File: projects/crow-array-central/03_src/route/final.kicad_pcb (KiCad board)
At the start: 6 copper layers, 176 x 122 mm, 238 parts, among them J1 RJHSE-5384, J10 INJ IN, J11 5V TERM DNP, J12 USB4105-GF-A, J13 xSYS DBG TDI/TDO, J14 xSYS DBG TMS/TCK, J2 RJHSE-5384, J3 RJHSE-5384, J4 RJHSE-5384, J5 RJHSE-5384, J6 RJHSE-5384, J7 RJHSE-5384 DNP, J8 RJHSE-5384 DNP, J9 DC-005 5V IN, Q1 AO3400A beep 1, Q2 AO3400A beep 2, Q3 AO3400A beep 3, Q4 AO3400A beep 4, Q5 AO3400A beep 5, Q6 AO3400A beep 6, Q7 AO3400A beep 7, Q8 AO3400A beep 8, Q9 AO3401A revFET, U1 XU316-1024-TQ128-I24, U10 AP61102 3V3, U11 AP61102 0V9, U12 TCR2LF18 1V8, U13 XC6227 3V3A, U2 PCM1865DBTR, U3 PCM1865DBTR, U4 W25Q16JVSSIQ, U5 NC7NZ34 MCLK buf, U6 SHT40-AD1B (0x44), Y1 FA-238 24MHz

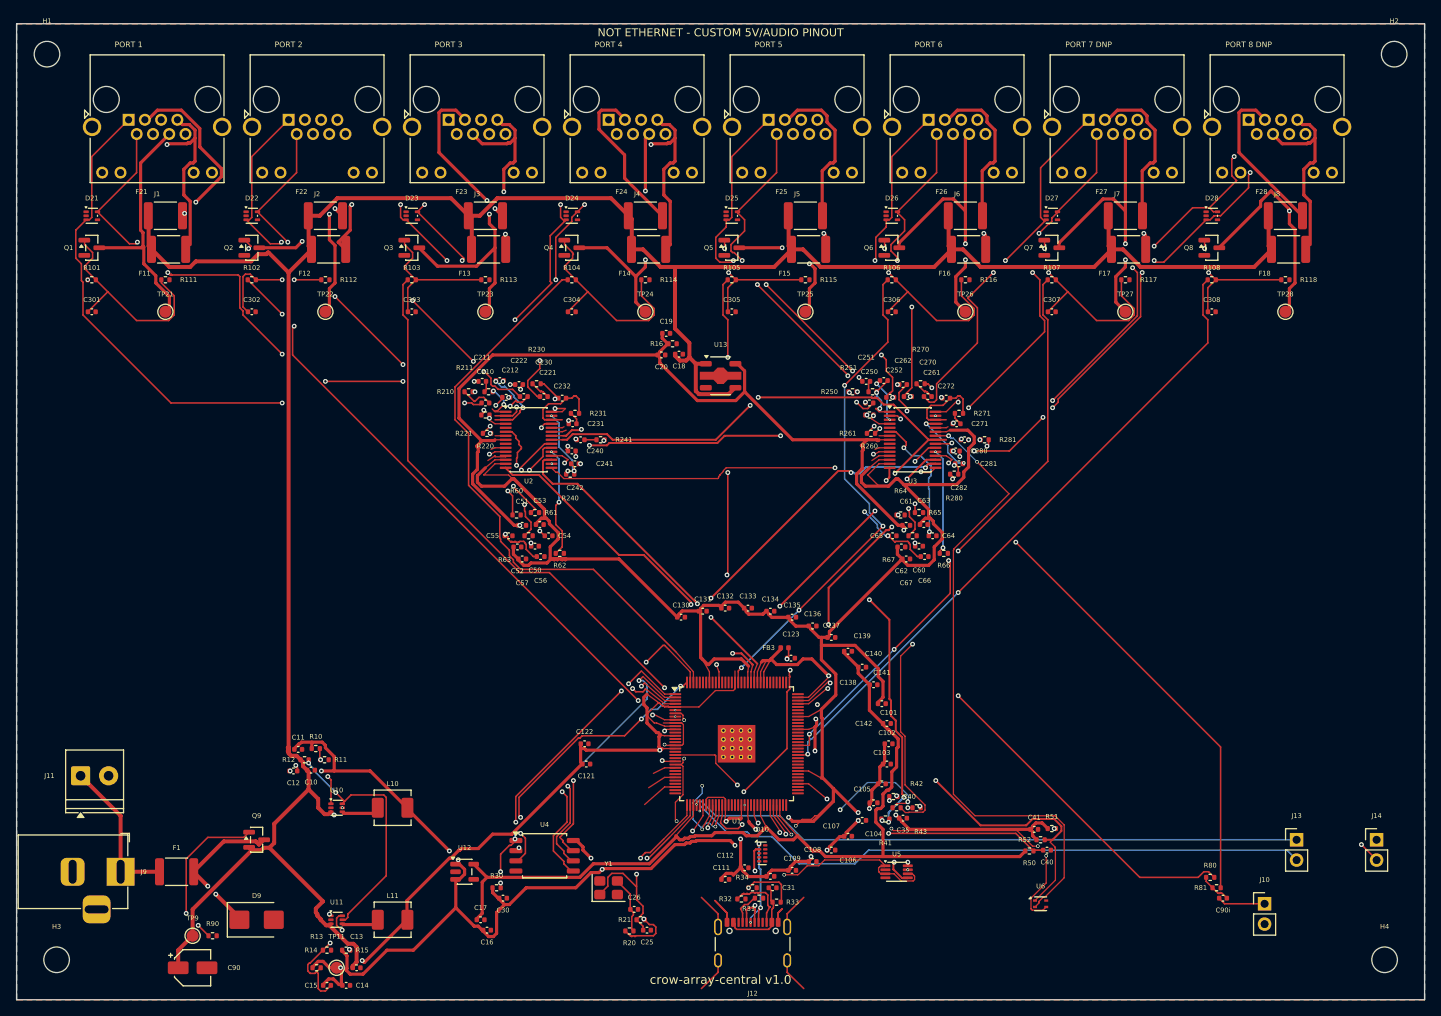
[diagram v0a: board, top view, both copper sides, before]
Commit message: crow-array-central: DRC GATE GREEN 0/0(waived-2)/0 — D25 power-neck exemption + D26 subprocess trim/clip
- neck_approaches.py (new, DRC-guarded): all 18 residual clearance items
  cleared by necking power segments to 0.20mm at unroutable approaches
  (cluster B: 5V at AP61102 0.5mm-pitch GND pads; A: 3V3 east trunk vs
  RST_N/MCLK_B/I2C escapes F.Cu+In3; C: 3V3 vs MCLK_A at R61), each under
  a scoped 'pwr_neck' rule area; generate_rules.py emits width_*_neck DRU
  exemptions (ampacity margin math in the DRU comment).
- trim_dangling.py rewritten SUBPROCESS-PER-EDIT (SWIG LoadBoard corruption)
  with clip-to-pad/via fallback: 10 of 11 spurs were load-bearing through-pin
  overshoots — clipped back to their covered pad (VB3P: grazed via) centers;
  1 pure spur removed. Dangling 11 -> 0.
- stitch_and_fill.py: width-lift pass exempts pwr_neck areas (was re-widening
  the necks); GND grid density gate counts TOTAL vias (idempotent on the
  promoted artifact).
- rebuild_all.sh: neck stage wired in; final gate encodes the ADR-0010
  zone-sliver waiver (max 2, Zone[GND]-only; anything else still fails).
- 03_src/route/final.kicad_pcb: fixed board promoted (canon M3); full chain
  re-run exit 0 with all guarded stages as no-ops.
- BRIEF: D25/D26 + DRC status now GATE GREEN.

Co-Authored-By: Claude Fable 5 <noreply@anthropic.com>
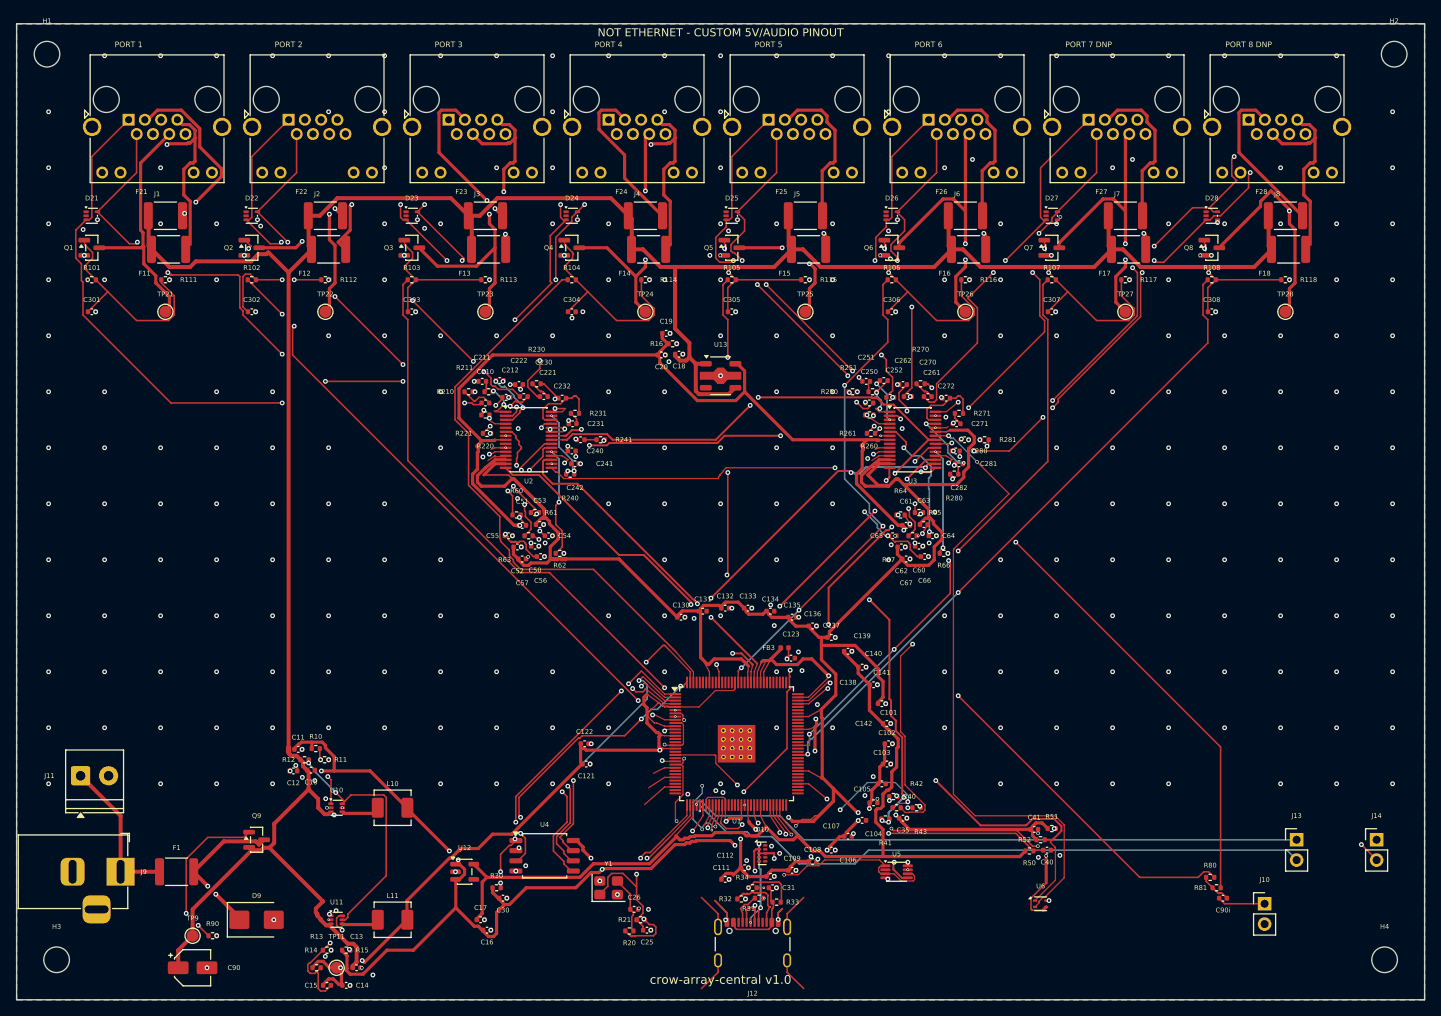
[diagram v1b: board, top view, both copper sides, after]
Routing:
- net GND: track 58.9 -> 68.2 mm, vias 0 -> 407
- net I2C_SCL: track 215.4 -> 217.0 mm
- net 0V9: track 220.3 -> 218.9 mm
- net VB3M: track 10.8 -> 9.42 mm
- net VA3M: track 10.8 -> 9.42 mm
- net VA2M: track 11.3 -> 9.97 mm
- net VA1P: track 12.6 -> 11.3 mm
- net I2C_SDA: track 144.7 -> 143.4 mm
- net 3V3: track 475.7 -> 474.4 mm
- net VB4M: track 14.1 -> 13.2 mm
- net VA4M: track 13.5 -> 12.6 mm
- net VA1M: track 7.27 -> 6.76 mm

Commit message: crow-array-central: release gates GREEN — stock/twin/pin-review/render/policy all pass
- bom_seed: 45 coded merged lines + 6 hand-solder; D27 substitutes (Y1
  FA-238->YXC X322524MOB4SI C70590 CL-12pF-identical; U12 TCR2LF18->TI
  TLV70018DDCR C79924 pin-compatible; C90 100u bulk RYVP6.3V100UF4*5
  C48970904 exact 4x5.4 land) with evidence part.yamls; stock verify
  >=5x qty5 clean except the designated XU316 consign line (C6938291).
- jlc_twin exit 0: 444 checks, zero mirrors, zero unadjudicated criticals;
  19-entry evidence-backed twin_adjudications.yaml (PAD-GEOM = ours-match-
  datasheet or generic-IPC lands; PAD-MISMATCH = duplicate-pad-number
  artifacts; ROT-DB deltas deferred to order preview per skill doctrine).
- fresh-context pin reviews 4/4 PASS (U1 129-pin no-mirror; PCM1865 pair;
  RJ45 group FAIL->adjudicated D28: board matches the SEALED pod v1.0
  terminal map 4=5V/5=GND/7=5V/8=GND — part.yaml doc error fixed, Q9
  class; U12/Y1 substitutes verified from TI/YXC primary figures).
- D29 add_silk_fn.py: 32 functional silk labels (J/F/TP), DRC-guarded,
  idempotent; audit_board I12 mate-direction + screw keepout (P-KEEP).
- policy_audit FULL: FAIL=0 (14 PASS, 3 WAIVED evidence-backed: R-DRC
  ADR-0010 slivers, R-POUR D15 floored-track ampacity math, R-THERM EP
  served by 16 footprint via-pads/I11), 6 HUMAN graded in render_review.
- render review PASS-WITH-NOTES, dispositions in 06_build/render_review.md.
- rebuild_all chain exit 0 from the promoted artifact, all stages no-op.

Co-Authored-By: Claude Fable 5 <noreply@anthropic.com>
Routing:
- net GND: vias 407 -> 411
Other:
- board text added: "2A PTC"
- board text added: "5V TERM DNP"
- board text added: "INJ IN"
- board text added: "PTC"
- board text added: "PTC audio 8"
- board text added: "PTC beep 8"
- board text added: "TP 0V9"
- board text added: "TP 5V"
- board text added: "TP BEEP_RET1"
- board text added: "TP BEEP_RET2"
- board text added: "TP BEEP_RET3"
- board text added: "TP BEEP_RET4"
- board text added: "TP BEEP_RET5"
- board text added: "TP BEEP_RET6"
- board text added: "TP BEEP_RET7"
- board text added: "TP BEEP_RET8"
- board text added: "xSYS DBG TDI/TDO"
